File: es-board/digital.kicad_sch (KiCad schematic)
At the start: 25 parts, among them J1 Conn_02x02_Odd_Even, Q5 NMOS, SW1 SW_SPST, SW2 SW_SPST, SW3 SW_SPST, SW4 SW_SPST, SW5 SW_SPST, U2 ATmega32U4-A, U5 OLED, Y1 16MHz Crystal

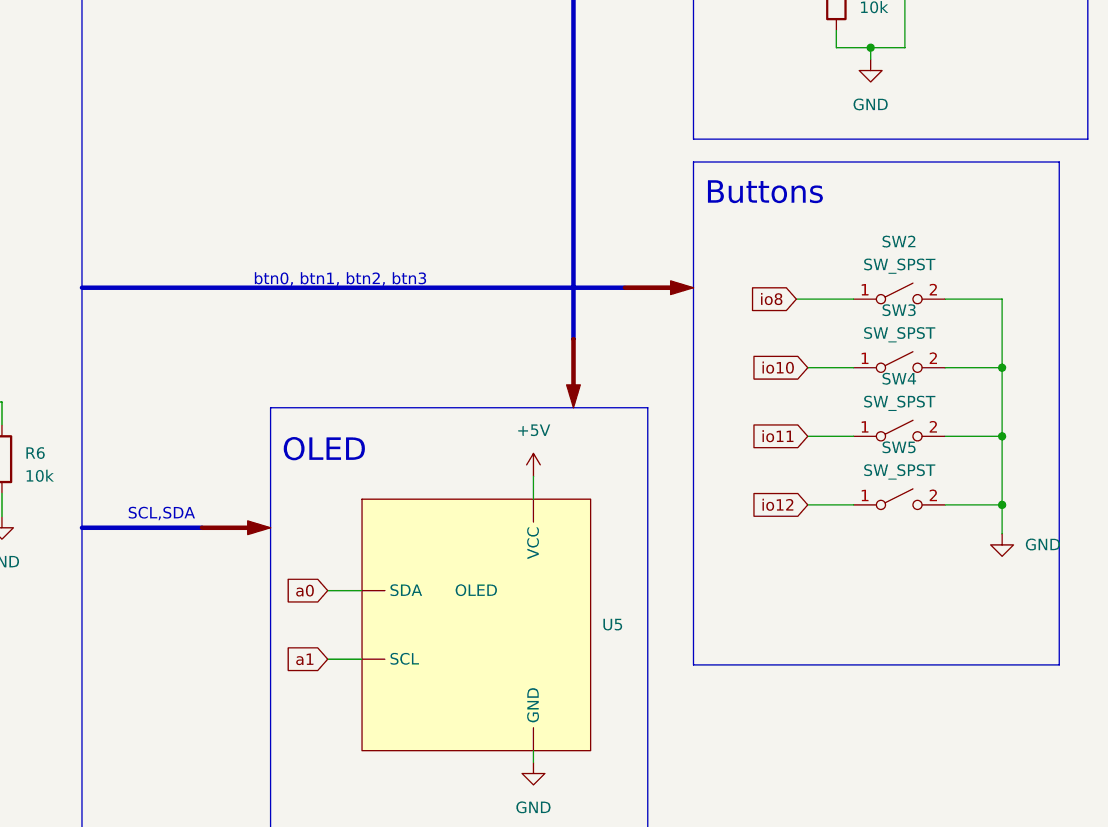
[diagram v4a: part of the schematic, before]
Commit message: Added net labels for buttons
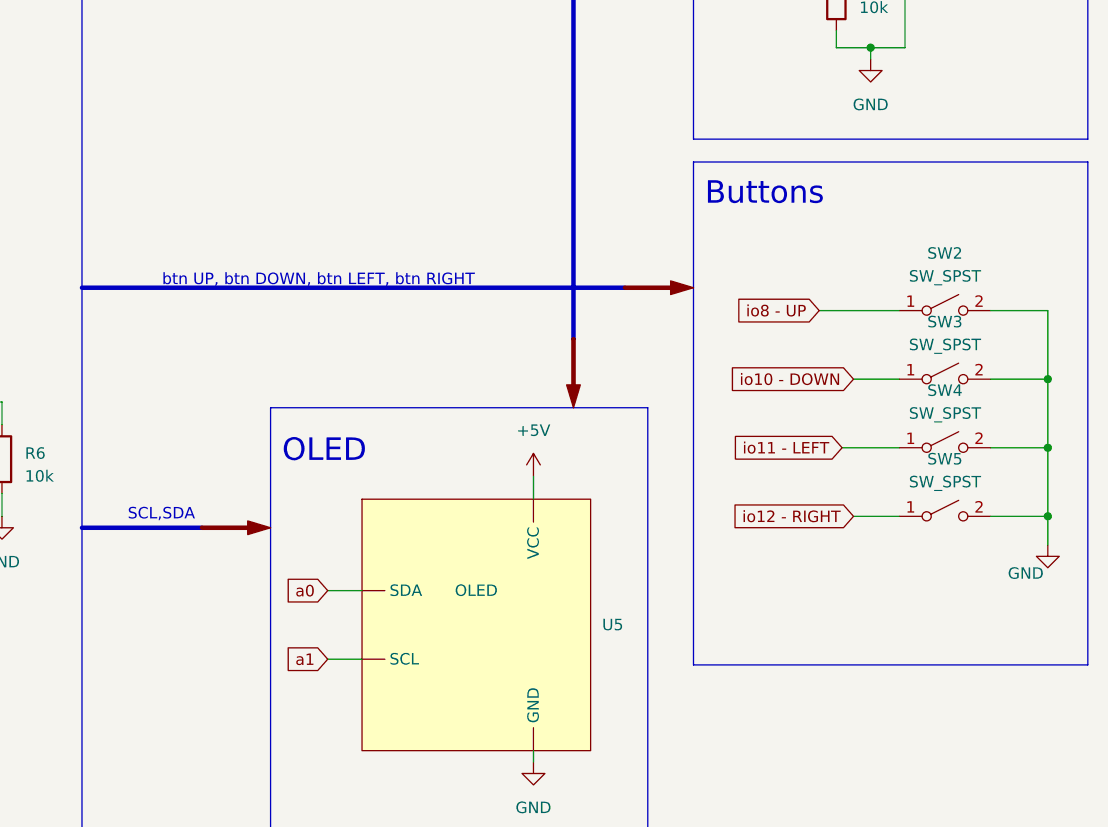
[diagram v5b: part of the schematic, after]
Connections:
- net io10: no longer SW3.1 (A)
- net io11: no longer SW4.1 (A)
- net io12: no longer SW5.1 (A)
- net io8: no longer SW2.1 (A)
- new net io10 - DOWN: SW3.1 (A)
- new net io11 - LEFT: SW4.1 (A)
- new net io12 - RIGHT: SW5.1 (A)
- new net io8 - UP: SW2.1 (A)
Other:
- note added: "btn UP, btn DOWN, btn LEFT, btn RIGHT"
- note removed: "btn0, btn1, btn2, btn3"
- moved on the sheet: SW2, SW3, SW4, SW5

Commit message: Updated footprints
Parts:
- C1, C2, C3, C4, C5, C6, C7: footprint Capacitor_SMD:C_0603_1608Metric -> Capacitor_SMD:C_1206_3216Metric
- C15: footprint (none) -> Connector_PinHeader_2.54mm:PinHeader_1x02_P2.54mm_Vertical
- D1, D2: footprint LED_SMD:LED_0603_1608Metric -> LED_SMD:LED_1206_3216Metric
- Q5: footprint (none) -> Package_TO_SOT_SMD:ATPAK-2
- R1, R6, R7, R8: footprint Resistor_SMD:R_0603_1608Metric -> Resistor_SMD:R_1206_3216Metric
- R14: footprint (none) -> Resistor_SMD:R_1206_3216Metric
- SW2, SW3, SW4, SW5: footprint (none) -> Button_Switch_SMD:SW_Push_1P1T_NO_6x6mm_H9.5mm
- U5: footprint (none) -> Connector_PinHeader_2.54mm:PinHeader_1x04_P2.54mm_Vertical
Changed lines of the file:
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@@
       (effects (font (size 1.27 1.27)) (justify right))
     )
-    (property "Footprint" "LED_SMD:LED_0603_1608Metric" (at 34.925 129.54 0)
+    (property "Footprint" "LED_SMD:LED_1206_3216Metric" (at 34.925 129.54 0)
       (effects (font (size 1.27 1.27)) hide)
     )
@@
       (effects (font (size 1.27 1.27)))
     )
-    (property "Footprint" "Capacitor_SMD:C_0603_1608Metric" (at 31.115 70.8152 0)
+    (property "Footprint" "Capacitor_SMD:C_1206_3216Metric" (at 31.115 70.8152 0)
       (effects (font (size 1.27 1.27)) hide)
     )
@@
       (effects (font (size 1.27 1.27)))
     )
-    (property "Footprint" "" (at 226.06 109.22 0)
+    (property "Footprint" "Button_Switch_SMD:SW_Push_1P1T_NO_6x6mm_H9.5mm" (at 226.06 109.22 0)
       (effects (font (size 1.27 1.27)) hide)
     )
@@
       (effects (font (size 1.27 1.27)) (justify left))
     )
-    (property "Footprint" "Capacitor_SMD:C_0603_1608Metric" (at 32.0802 100.33 0)
+    (property "Footprint" "Capacitor_SMD:C_1206_3216Metric" (at 32.0802 100.33 0)
       (effects (font (size 1.27 1.27)) hide)
     )
@@
       (effects (font (size 1.27 1.27)) (justify right))
     )
-    (property "Footprint" "" (at 215.773 66.675 90)
+    (property "Footprint" "Resistor_SMD:R_1206_3216Metric" (at 215.773 66.675 90)
       (effects (font (size 1.27 1.27)) hide)
     )
@@
       (effects (font (size 1.27 1.27)) (justify left))
     )
-    (property "Footprint" "Resistor_SMD:R_0603_1608Metric" (at 59.817 54.61 90)
+    (property "Footprint" "Resistor_SMD:R_1206_3216Metric" (at 59.817 54.61 90)
       (effects (font (size 1.27 1.27)) hide)
     )
@@
       (effects (font (size 1.27 1.27)) (justify left))
     )
-    (property "Footprint" "Capacitor_SMD:C_0603_1608Metric" (at 54.9402 58.42 0)
+    (property "Footprint" "Capacitor_SMD:C_1206_3216Metric" (at 54.9402 58.42 0)
       (effects (font (size 1.27 1.27)) hide)
     )
@@
       (effects (font (size 1.27 1.27)))
     )
-    (property "Footprint" "" (at 226.06 116.84 0)
+    (property "Footprint" "Button_Switch_SMD:SW_Push_1P1T_NO_6x6mm_H9.5mm" (at 226.06 116.84 0)
       (effects (font (size 1.27 1.27)) hide)
     )
@@
       (effects (font (size 1.27 1.27)) (justify left))
     )
-    (property "Footprint" "Capacitor_SMD:C_0603_1608Metric" (at 61.2902 102.87 0)
+    (property "Footprint" "Capacitor_SMD:C_1206_3216Metric" (at 61.2902 102.87 0)
       (effects (font (size 1.27 1.27)) hide)
     )
@@
       (effects (font (size 1.27 1.27)) (justify right))
     )
-    (property "Footprint" "LED_SMD:LED_0603_1608Metric" (at 50.165 139.7 0)
+    (property "Footprint" "LED_SMD:LED_1206_3216Metric" (at 50.165 139.7 0)
       (effects (font (size 1.27 1.27)) hide)
     )
@@
       (effects (font (size 1.27 1.27)))
     )
-    (property "Footprint" "" (at 226.06 101.6 0)
+    (property "Footprint" "Button_Switch_SMD:SW_Push_1P1T_NO_6x6mm_H9.5mm" (at 226.06 101.6 0)
       (effects (font (size 1.27 1.27)) hide)
     )
@@
       (effects (font (size 1.27 1.27)))
     )
-    (property "Footprint" "Capacitor_SMD:C_0603_1608Metric" (at 31.115 63.1952 0)
+    (property "Footprint" "Capacitor_SMD:C_1206_3216Metric" (at 31.115 63.1952 0)
       (effects (font (size 1.27 1.27)) hide)
     )
@@
       (effects (font (size 1.27 1.27)) (justify left))
     )
-    (property "Footprint" "Resistor_SMD:R_0603_1608Metric" (at 48.387 129.54 90)
+    (property "Footprint" "Resistor_SMD:R_1206_3216Metric" (at 48.387 129.54 90)
       (effects (font (size 1.27 1.27)) hide)
     )
@@
       (effects (font (size 1.27 1.27)) (justify left))
     )
-    (property "Footprint" "" (at 222.5802 52.705 0)
+    (property "Footprint" "Connector_PinHeader_2.54mm:PinHeader_1x02_P2.54mm_Vertical" (at 222.5802 52.705 0)
       (effects (font (size 1.27 1.27)) hide)
     )
@@
       (effects (font (size 1.27 1.27)) (justify left))
     )
-    (property "Footprint" "Capacitor_SMD:C_0603_1608Metric" (at 44.7802 100.33 0)
+    (property "Footprint" "Capacitor_SMD:C_1206_3216Metric" (at 44.7802 100.33 0)
       (effects (font (size 1.27 1.27)) hide)
     )
@@
       (effects (font (size 1.27 1.27)) (justify left))
     )
-    (property "Footprint" "" (at 224.155 57.15 0)
+    (property "Footprint" "Package_TO_SOT_SMD:ATPAK-2" (at 224.155 57.15 0)
       (effects (font (size 1.27 1.27)) hide)
     )
@@
       (effects (font (size 1.27 1.27)) (justify left))
     )
-    (property "Footprint" "Resistor_SMD:R_0603_1608Metric" (at 119.507 118.11 90)
+    (property "Footprint" "Resistor_SMD:R_1206_3216Metric" (at 119.507 118.11 90)
       (effects (font (size 1.27 1.27)) hide)
     )
@@
       (effects (font (size 1.27 1.27)) (justify left))
     )
-    (property "Footprint" "Resistor_SMD:R_0603_1608Metric" (at 33.147 139.7 90)
+    (property "Footprint" "Resistor_SMD:R_1206_3216Metric" (at 33.147 139.7 90)
       (effects (font (size 1.27 1.27)) hide)
     )
@@
       (effects (font (size 1.27 1.27)))
     )
-    (property "Footprint" "" (at 226.06 124.46 0)
+    (property "Footprint" "Button_Switch_SMD:SW_Push_1P1T_NO_6x6mm_H9.5mm" (at 226.06 124.46 0)
       (effects (font (size 1.27 1.27)) hide)
     )
@@
       (effects (font (size 1.27 1.27)))
     )
-    (property "Footprint" "Capacitor_SMD:C_0603_1608Metric" (at 52.705 74.6252 0)
+    (property "Footprint" "Capacitor_SMD:C_1206_3216Metric" (at 52.705 74.6252 0)
       (effects (font (size 1.27 1.27)) hide)
     )
@@
       (effects (font (size 1.27 1.27)))
     )
-    (property "Footprint" "" (at 173.99 132.715 0)
-      (effects (font (size 1.27 1.27)) hide)
-    )
+    (property "Footprint" "Connector_PinHeader_2.54mm:PinHeader_1x04_P2.54mm_Vertical" (at 173.99 132.715 0)
+      (effects (font (size 1.27 1.27)) hide)
+    )

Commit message: Preliminary layout completed
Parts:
- J1: footprint Library:PinHeader1.28-Pads-2x2_1 -> Connector_PinHeader_2.54mm:PinHeader_1x04_P2.54mm_Vertical
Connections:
- net +5V: now also U5.2 (VCC); no longer U5. (VCC)
- net GND: now also U5.1 (GND); no longer U5. (VCC)
- net a0: now also U5.4 (SDA); no longer U5. (VCC)
- net a1: now also U5.3 (SCL); no longer U5. (VCC)
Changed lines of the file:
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@@
       (effects (font (size 1.27 1.27)))
     )
-    (property "Footprint" "Library:PinHeader1.28-Pads-2x2_1" (at 62.865 156.21 0)
+    (property "Footprint" "Connector_PinHeader_2.54mm:PinHeader_1x04_P2.54mm_Vertical" (at 62.865 156.21 0)
       (effects (font (size 1.27 1.27)) hide)
     )
@@
       (effects (font (size 1.27 1.27)) hide)
     )
-    (pin "")
-    (pin "")
-    (pin "")
-    (pin "")
-    (instances
-      (project "es-board"
+    (pin "1")
+    (pin "2")
+    (pin "3")
+    (pin "4")
+    (instances
+      (project "es-board"

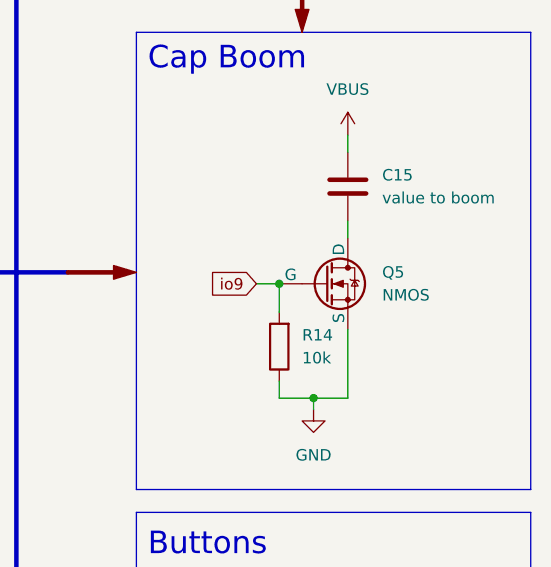
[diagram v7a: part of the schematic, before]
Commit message: Picked boom MOSFET
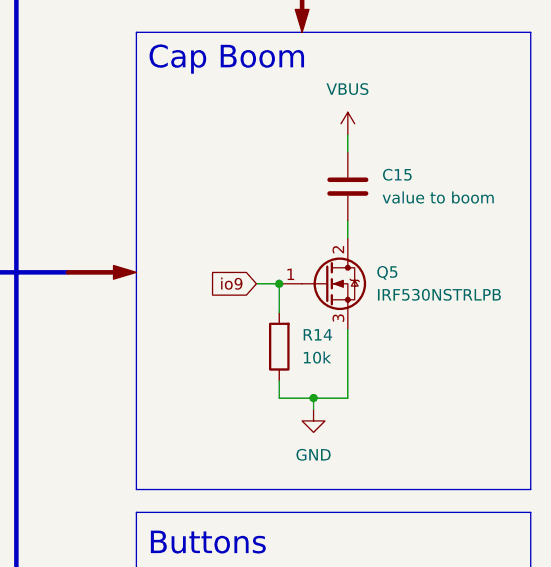
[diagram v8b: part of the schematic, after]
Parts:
- Q5: value NMOS -> IRF530NSTRLPB; footprint Package_TO_SOT_SMD:ATPAK-2 -> explosnake:TO-263-2_TabPin2; symbol Simulation_SPICE:NMOS -> Device:Q_NMOS_GDS; DPN (none) -> IRF530NSTRLPBFCT-ND; MPN (none) -> IRF530NSTRLPBF
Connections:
- net io9: now also Q5.1 (G); no longer Q5.2 (G)
- net at C15.2: now also Q5.2 (D); no longer Q5.1 (D)
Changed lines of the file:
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@@
     )
   )
-  (symbol (lib_id "Simulation_SPICE:NMOS") (at 219.075 59.69 0) (unit 1)
+  (symbol (lib_id "Device:Q_NMOS_GDS") (at 219.075 59.69 0) (unit 1)
     (in_bom yes) (on_board yes) (dnp no) (fields_autoplaced)
-    (property "Reference" "Q5" (at 225.425 58.42 0)
+    (property "Reference" "Q5" (at 224.79 58.42 0)
       (effects (font (size 1.27 1.27)) (justify left))
     )
-    (property "Value" "NMOS" (at 225.425 60.96 0)
+    (property "Value" "IRF530NSTRLPB" (at 224.79 60.96 0)
       (effects (font (size 1.27 1.27)) (justify left))
     )
-    (property "Footprint" "Package_TO_SOT_SMD:ATPAK-2" (at 224.155 57.15 0)
+    (property "Footprint" "explosnake:TO-263-2_TabPin2" (at 224.155 57.15 0)
       (effects (font (size 1.27 1.27)) hide)
     )
-    (property "Datasheet" "https://ngspice.sourceforge.io/docs/ngspice-manual.pdf" (at 219.075 72.39 0)
+    (property "Datasheet" "https://www.infineon.com/dgdl/irf530nspbf.pdf?fileId=5546d462533600a4015355e38eb4199c" (at 219.075 59.69 0)
       (effects (font (size 1.27 1.27)) hide)
     )
@@
       (effects (font (size 1.27 1.27)) hide)
     )
+    (property "DPN" "IRF530NSTRLPBFCT-ND" (at 219.075 59.69 0)
+      (effects (font (size 1.27 1.27)) hide)
+    )
+    (property "MPN" "IRF530NSTRLPBF" (at 219.075 59.69 0)
+      (effects (font (size 1.27 1.27)) hide)
+    )
